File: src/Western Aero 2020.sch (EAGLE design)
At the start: 78 parts, among them IC1 7805DT, IC3 7806DT

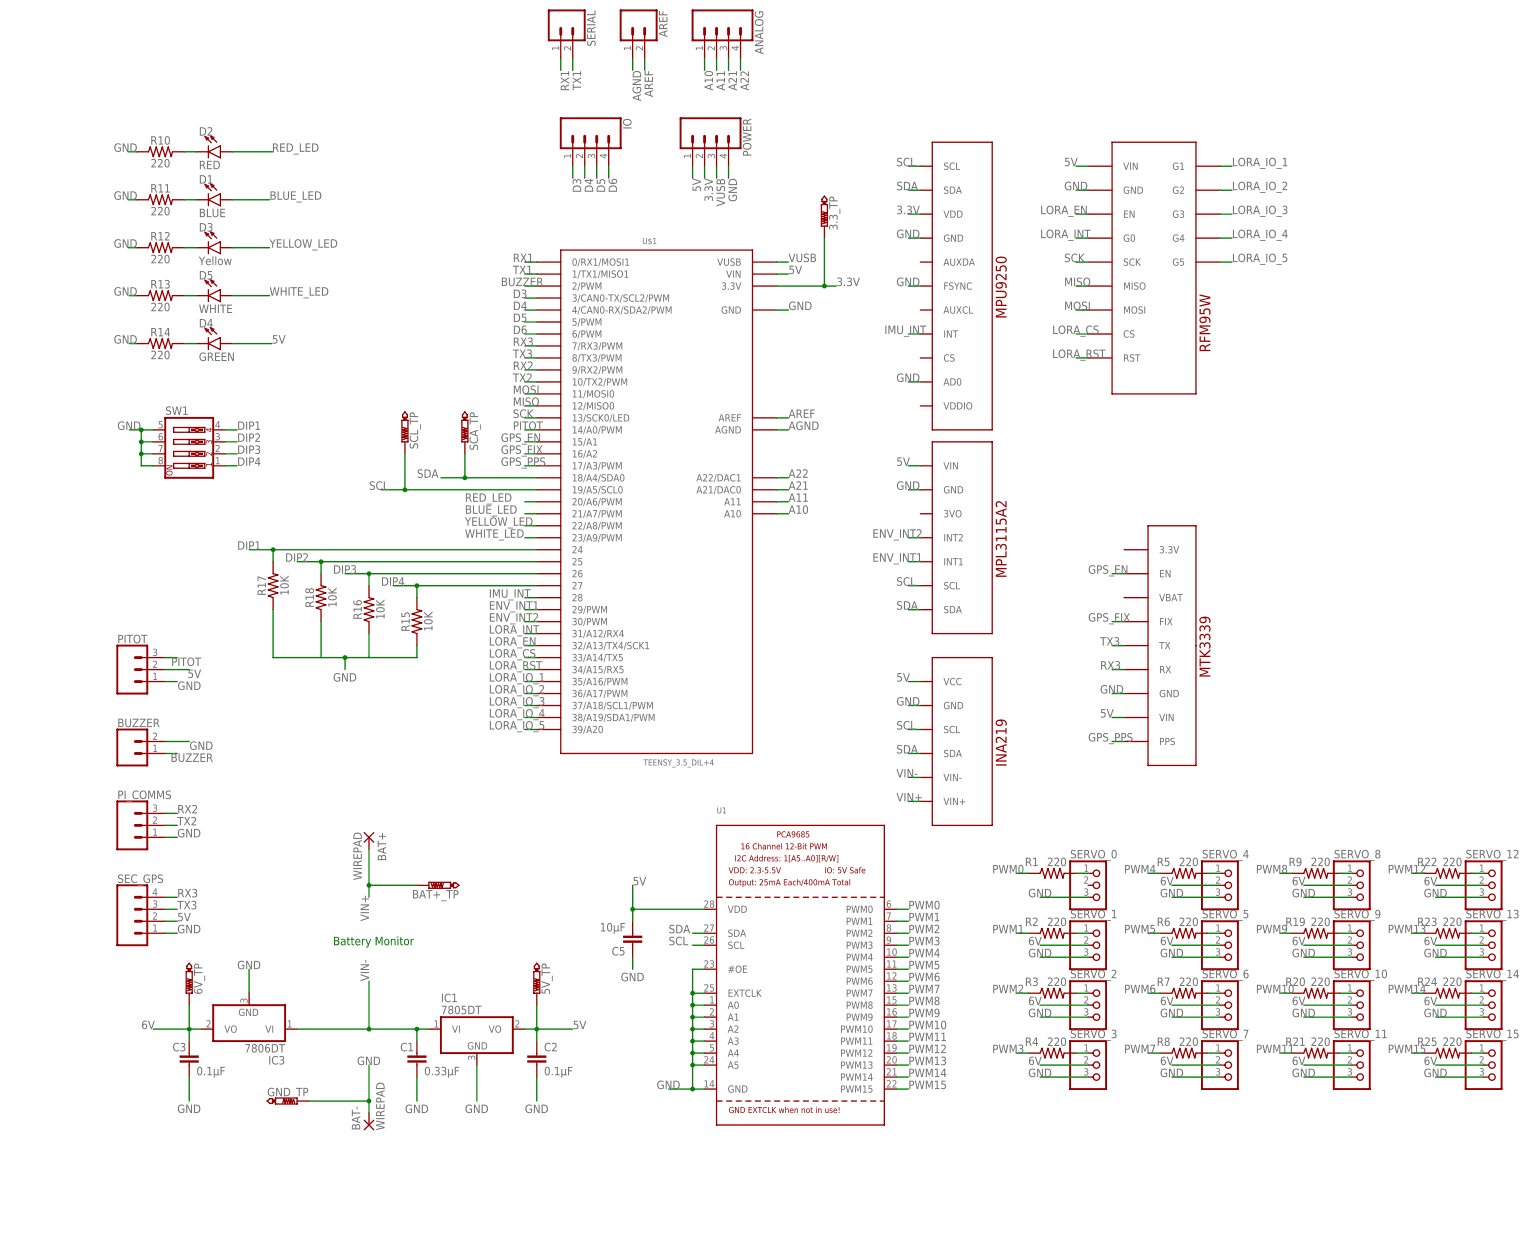
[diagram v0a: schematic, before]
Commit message: Rewired radio
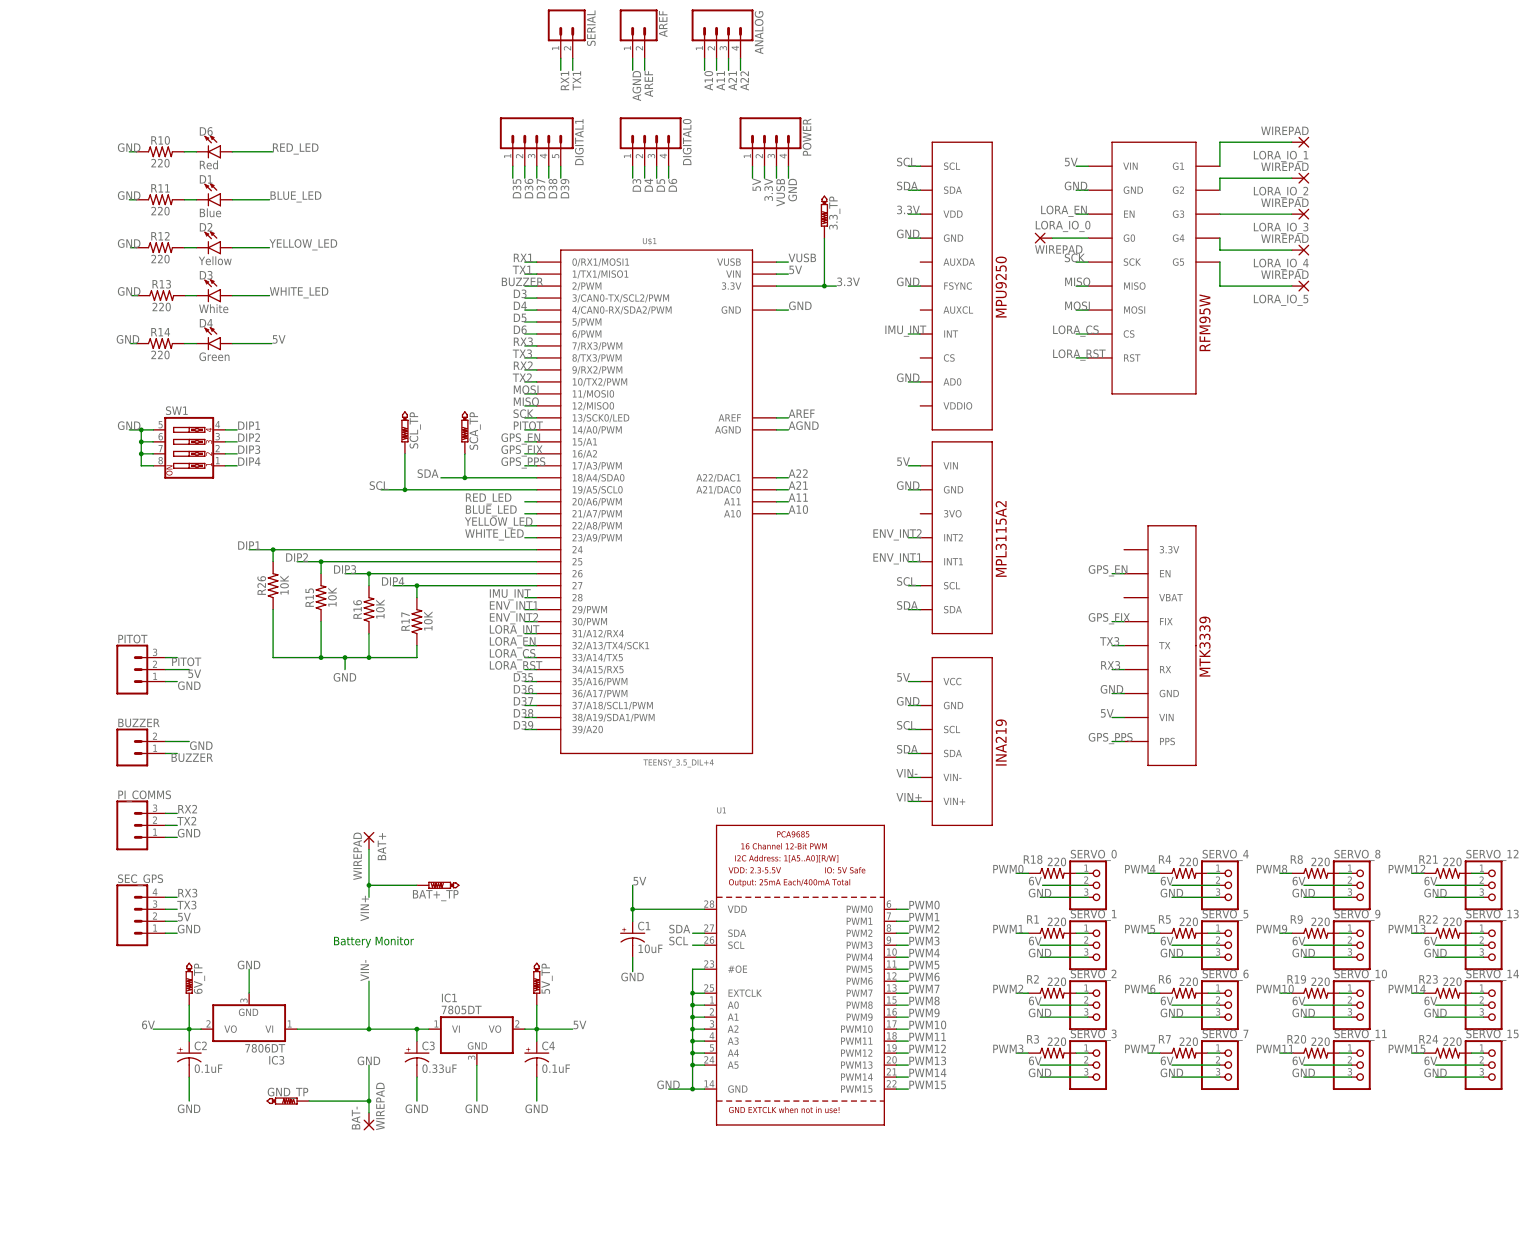
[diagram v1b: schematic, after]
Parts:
- removed C5: 10µF, SparkFun-Capacitors:0.33UF/330NF-0805-50V-10%
- removed D5: WHITE, SparkFun-LED:LED-WHITE0603
- removed IO: (no value), SparkFun-Connectors:CONN_04
- removed R25: 220, SparkFun-Resistors:0.3OHM-0805-1/8W-1%
- added C4: 0.1uF, SparkFun-Capacitors:10UF-POLAR-RADIAL-2.5MM-25V-20%
- added D6: Red, SparkFun-LED:LED3MM
- added DIGITAL0: (no value), SparkFun-Connectors:CONN_04
- added DIGITAL1: (no value), SparkFun-Connectors:CONN_05
- added LORA_IO_0, LORA_IO_1, LORA_IO_2, LORA_IO_3, LORA_IO_4, LORA_IO_5: WIREPAD, wirepad:WIREPAD2,15/1,0
- added R26: 10K, SparkFun-Resistors:330OHM-HORIZ-1/10W-5%
- C1: value 0.33µF -> 10uF; device SparkFun-Capacitors:0.33UF/330NF-0805-50V-10% -> SparkFun-Capacitors:10UF-POLAR-RADIAL-2.5MM-25V-20%
- C2: value 0.1µF -> 0.1uF; device SparkFun-Capacitors:0.33UF/330NF-0805-50V-10% -> SparkFun-Capacitors:10UF-POLAR-RADIAL-2.5MM-25V-20%
- C3: value 0.1µF -> 0.33uF; device SparkFun-Capacitors:0.33UF/330NF-0805-50V-10% -> SparkFun-Capacitors:10UF-POLAR-RADIAL-2.5MM-25V-20%
- D1: value BLUE -> Blue; device SparkFun-LED:LED-BLUE0603 -> SparkFun-LED:LED3MM
- D2: value RED -> Yellow; device SparkFun-LED:LED-RED0603 -> SparkFun-LED:LED3MM
- D3: value Yellow -> White; device SparkFun-LED:LED-YELLOW0603 -> SparkFun-LED:LED3MM
- D4: value GREEN -> Green; device SparkFun-LED:LED-GREEN0603 -> SparkFun-LED:LED3MM
- R1, R10, R11, R12, R13, R14, R15, R16, R17, R19, R2, R20, R21, R22, R23, R24, R3, R4, R5, R6, R7, R8, R9: device SparkFun-Resistors:0.3OHM-0805-1/8W-1% -> SparkFun-Resistors:330OHM-HORIZ-1/10W-5%
- R18: value 10K -> 220; device SparkFun-Resistors:0.3OHM-0805-1/8W-1% -> SparkFun-Resistors:330OHM-HORIZ-1/10W-5%
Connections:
- removed net LORA_IO_1: U$1.35/A16/PWM, U$3.G1
- removed net LORA_IO_2: U$1.36/A17/PWM, U$3.G2
- removed net LORA_IO_3: U$1.37/A18/SCL1/PWM, U$3.G3
- removed net LORA_IO_4: U$1.38/A19/SDA1/PWM, U$3.G4
- removed net LORA_IO_5: U$1.39/A20, U$3.G5
- removed net N$3 (its old number): D2.C, R10.2
- removed net N$6 (its old number): D3.C, R12.2
- new net D35: DIGITAL1.1, U$1.35/A16/PWM
- new net D36: DIGITAL1.2, U$1.36/A17/PWM
- new net D37: DIGITAL1.3, U$1.37/A18/SCL1/PWM
- new net D38: DIGITAL1.4, U$1.38/A19/SDA1/PWM
- new net D39: DIGITAL1.5, U$1.39/A20
- new net N$10: LORA_IO_2.P, U$3.G2
- new net N$25: LORA_IO_4.P, U$3.G4
- new net N$26: LORA_IO_3.P, U$3.G3
- new net N$27: LORA_IO_0.P, U$3.G0
- new net N$5: D3.C, R13.2
- new net N$8: LORA_IO_1.P, U$3.G1
- net 5V: now also C1.+, C4.+; no longer C2.1, C5.2
- net 6V: now also C2.+, SERVO_0.2; no longer C3.1
- net D3: now also DIGITAL0.1; no longer IO.1
- net D4: now also DIGITAL0.2; no longer IO.2
- net D5: now also DIGITAL0.3; no longer IO.3
- net D6: now also DIGITAL0.4; no longer IO.4
- net DIP1: now also R26.2; no longer R17.2
- net DIP2: now also R15.2; no longer R18.2
- net DIP4: now also R17.2; no longer R15.2
- net GND: now also C1.-, C2.-, C3.-, C4.-, R16.1, R26.1; no longer C1.2, C2.2, C3.2, C5.1
- net LORA_INT: no longer U$3.G0
- net N$1: now also R18.2; no longer R1.2
- net N$11: now also R2.2; no longer R3.2
- net N$12: now also R3.2; no longer R4.2
- net N$13: now also R4.2; no longer R5.2
- net N$14: now also R5.2; no longer R6.2
- net N$15: now also R6.2; no longer R7.2
- net N$16: now also R7.2; no longer R8.2
- net N$17: now also R8.2; no longer R9.2
- net N$18: now also R9.2; no longer R19.2
- net N$19: now also R19.2; no longer R20.2
- net N$2: now also D6.C, R10.2; no longer R18.1
- net N$20: now also R20.2; no longer R21.2
- net N$21: now also R21.2; no longer R22.2
- net N$22: now also R22.2; no longer R23.2
- net N$23: now also R23.2; no longer R24.2
- net N$24: now also R24.2; no longer R25.2
- net N$4: now also D2.C, R12.2; no longer R16.1
- net N$7: now also LORA_IO_5.P, U$3.G5; no longer D5.C, R13.2
- net N$9: now also R1.2; no longer R2.2
- net PWM0: now also R18.1; no longer R1.1
- net PWM1: now also R1.1; no longer R2.1
- net PWM10: now also R19.1; no longer R20.1
- net PWM11: now also R20.1; no longer R21.1
- net PWM12: now also R21.1; no longer R22.1
- net PWM13: now also R22.1; no longer R23.1
- net PWM14: now also R23.1; no longer R24.1
- net PWM15: now also R24.1; no longer R25.1
- net PWM2: now also R2.1; no longer R3.1
- net PWM3: now also R3.1; no longer R4.1
- net PWM4: now also R4.1; no longer R5.1
- net PWM5: now also R5.1; no longer R6.1
- net PWM6: now also R6.1; no longer R7.1
- net PWM7: now also R7.1; no longer R8.1
- net PWM8: now also R8.1; no longer R9.1
- net PWM9: now also R9.1; no longer R19.1
- net RED_LED: now also D6.A; no longer D2.A
- net VIN-: now also C3.+; no longer C1.1
- net WHITE_LED: now also D3.A; no longer D5.A
- net YELLOW_LED: now also D2.A; no longer D3.A
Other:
- moved on the sheet: D2, D3, POWER, R1, R15, R17, R18, R19, R2, R20, R21, R22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

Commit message: Added screwholes, adjusted addresses, few other tweaks
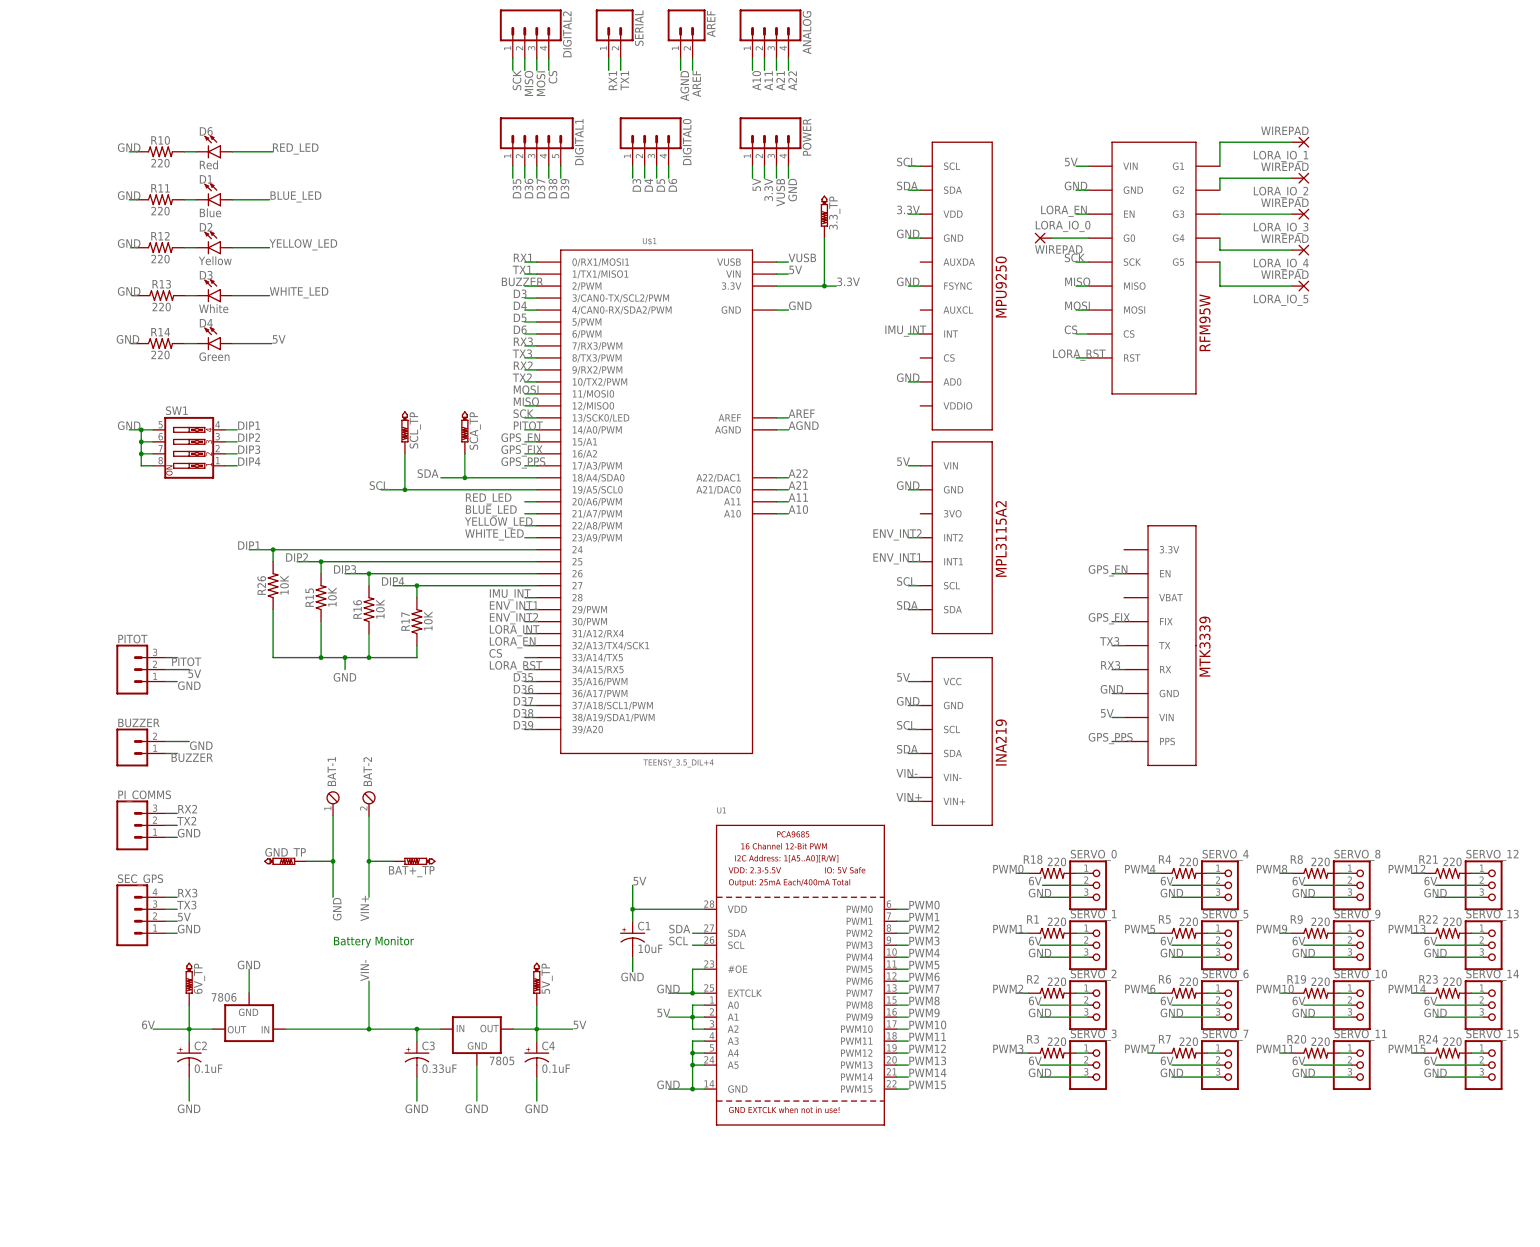
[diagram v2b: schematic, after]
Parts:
- removed BAT+, BAT-: WIREPAD, wirepad:WIREPAD2,15/1,0
- removed IC1: 7805DT, linear:7805DT
- removed IC3: 7806DT, linear:7806DT
- added 7805, 7806: (no value), SparkFun-IC-Power:V_REG_78XXSINK
- added BAT: (no value), con-phoenix-254:MPT2
- added DIGITAL2: (no value), SparkFun-Connectors:CONN_04
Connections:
- removed net LORA_CS: U$1.33/A14/TX5, U$3.CS
- new net CS: DIGITAL2.4, U$1.33/A14/TX5, U$3.CS
- net 5V: now also 7805.OUT, U1.A0, U1.A1, U1.A2; no longer IC1.VO
- net 6V: now also 7806.OUT; no longer IC3.VO
- net GND: now also 7805.GND, 7806.GND, BAT-1.1; no longer BAT-.P, IC1.GND, IC3.GND, U1.A0, U1.A1, U1.A2
- net MISO: now also DIGITAL2.2
- net MOSI: now also DIGITAL2.3
- net SCK: now also DIGITAL2.1
- net VIN+: now also BAT-2.1; no longer BAT+.P
- net VIN-: now also 7805.IN, 7806.IN; no longer IC1.VI, IC3.VI
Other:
- moved on the sheet: ANALOG, AREF, BAT+_TP, GND_TP, SERIAL

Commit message: new layout
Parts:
- removed 7806: (no value), SparkFun-IC-Power:V_REG_78XXSINK
- removed D6: Red, SparkFun-LED:LED3MM
- removed R26: 10K, SparkFun-Resistors:330OHM-HORIZ-1/10W-5%
- added D5: Green, SparkFun-LED:LED3MM
- added R25: 220, SparkFun-Resistors:330OHM-HORIZ-1/10W-5%
- added U4: (no value), adafruit:PCA9685
- C1: value 10uF -> 0.1uF
- C2: value 0.1uF -> 0.33uF
- C3: value 0.33uF -> 0.1uF
- C4: value 0.1uF -> 10uF
- D1: value Blue -> Red
- D2: value Yellow -> Blue
- D3: value White -> Yellow
- D4: value Green -> White
- R15, R16, R17: value 10K -> 220
- R6, R7, R8, R9: value 220 -> 10K
- U1: value (none) -> 7806; device adafruit:PCA9685 -> SparkFun-IC-Power:V_REG_78XXSINK
- U2: value (none) -> 7805
- renumbered 3.3_TP to TP7, 5V_TP to TP6, 6V_TP to TP1, 7805 to U2, ANALOG to J10, AREF to J9, BAT to X1, BAT+_TP to TP4, BUZZER to J2, DIGITAL0 to J8, DIGITAL1 to J6, DIGITAL2 to J5, GND_TP to TP2, LORA_IO_0 to PAD1, LORA_IO_1 to PAD2, LORA_IO_2 to PAD3, LORA_IO_3 to PAD4, LORA_IO_4 to PAD5, LORA_IO_5 to PAD6, PITOT to J1, PI_COMMS to J3, POWER to J11, SCA_TP to TP5, SCL_TP to TP3, SEC_GPS to J4, SERIAL to J7, SERVO_0 to JP1, SERVO_1 to JP2, SERVO_10 to JP11, SERVO_11 to JP12, SERVO_12 to JP13, SERVO_13 to JP14, SERVO_14 to JP15, SERVO_15 to JP16, SERVO_2 to JP3, SERVO_3 to JP4, SERVO_4 to JP5, SERVO_5 to JP6, SERVO_6 to JP7, SERVO_7 to JP8, SERVO_8 to JP9, SERVO_9 to JP10, U$1 to U3, U$2 to U5, U$3 to U8, U$4 to U6, U$5 to U7, U$6 to U9
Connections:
- net 5V: now also C3.+, D5.A, U4.A0, U4.A1, U4.A2, U4.VDD; no longer C1.+, D4.A, U1.A0, U1.A1, U1.A2, U1.VDD
- net 6V: now also C1.+, U1.OUT; no longer 7806.OUT, C2.+
- net BLUE_LED: now also D2.A; no longer D1.A
- net DIP1: now also R6.2; no longer R26.2
- net DIP2: now also R7.2; no longer R15.2
- net DIP3: now also R8.2; no longer R16.2
- net DIP4: now also R9.2; no longer R17.2
- net GND: now also R1.1, R2.1, R3.1, R4.1, R5.1, R6.1, R7.1, R8.1, R9.1, U4.#OE, U4.A3, U4.A4, U4.A5, U4.EXTCLK, U4.GND; no longer 7806.GND, R10.1, R11.1, R12.1, R13.1, R14.1, R15.1, R16.1, R17.1, R26.1, U1.#OE, U1.A3, U1.A4, U1.A5, U1.EXTCLK
- net N$1: now also R10.2; no longer R18.2
- net N$11: now also R12.2; no longer R2.2
- net N$12: now also R13.2; no longer R3.2
- net N$13: now also R14.2; no longer R4.2
- net N$14: now also R15.2; no longer R5.2
- net N$15: now also R16.2; no longer R6.2
- net N$16: now also R17.2; no longer R7.2
- net N$17: now also R18.2; no longer R8.2
- net N$18: now also R19.2; no longer R9.2
- net N$19: now also R20.2; no longer R19.2
- net N$2: now also D1.C, R1.2; no longer D6.C, R10.2
- net N$20: now also R21.2; no longer R20.2
- net N$21: now also R22.2; no longer R21.2
- net N$22: now also R23.2; no longer R22.2
- net N$23: now also R24.2; no longer R23.2
- net N$24: now also R25.2; no longer R24.2
- net N$3: now also D2.C, R2.2; no longer D1.C, R11.2
- net N$4: now also D3.C, R3.2; no longer D2.C, R12.2
- net N$5: now also D4.C, R5.2; no longer D3.C, R13.2
- net N$6: now also D5.C, R4.2; no longer D4.C, R14.2
- net N$9: now also R11.2; no longer R1.2
- net PWM0: now also R10.1, U4.PWM0; no longer R18.1, U1.PWM0
- net PWM1: now also R11.1, U4.PWM1; no longer R1.1, U1.PWM1
- net PWM10: now also R20.1, U4.PWM10; no longer R19.1, U1.PWM10
- net PWM11: now also R21.1, U4.PWM11; no longer R20.1, U1.PWM11
- net PWM12: now also R22.1, U4.PWM12; no longer R21.1, U1.PWM12
- net PWM13: now also R23.1, U4.PWM13; no longer R22.1, U1.PWM13
- net PWM14: now also R24.1, U4.PWM14; no longer R23.1, U1.PWM14
- net PWM15: now also R25.1, U4.PWM15; no longer R24.1, U1.PWM15
- net PWM2: now also R12.1, U4.PWM2; no longer R2.1, U1.PWM2
- net PWM3: now also R13.1, U4.PWM3; no longer R3.1, U1.PWM3
- net PWM4: now also R14.1, U4.PWM4; no longer R4.1, U1.PWM4
- net PWM5: now also R15.1, U4.PWM5; no longer R5.1, U1.PWM5
- net PWM6: now also R16.1, U4.PWM6; no longer R6.1, U1.PWM6
- net PWM7: now also R17.1, U4.PWM7; no longer R7.1, U1.PWM7
- net PWM8: now also R18.1, U4.PWM8; no longer R8.1, U1.PWM8
- net PWM9: now also R19.1, U4.PWM9; no longer R9.1, U1.PWM9
- net RED_LED: now also D1.A; no longer D6.A
- net SCL: now also U4.SCL; no longer U1.SCL
- net SDA: now also U4.SDA; no longer U1.SDA
- net VIN-: now also C2.+, U1.IN; no longer 7806.IN, C3.+
- net WHITE_LED: now also D4.A; no longer D3.A
- net YELLOW_LED: now also D3.A; no longer D2.A
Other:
- moved on the sheet: C1, C2, C3, C4, D1, D2, D3, D4, R1, R10, R11, R12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
